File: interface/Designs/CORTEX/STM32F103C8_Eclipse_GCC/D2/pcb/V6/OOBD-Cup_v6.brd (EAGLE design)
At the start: 160 x 100 mm, 42 parts, among them IC1 MC34063-SO, IC2 BTM-182, IC3 PCA82C250T, T1 BC817, T100 BC817, T101 BC817, U1 STM32F10XTXU6

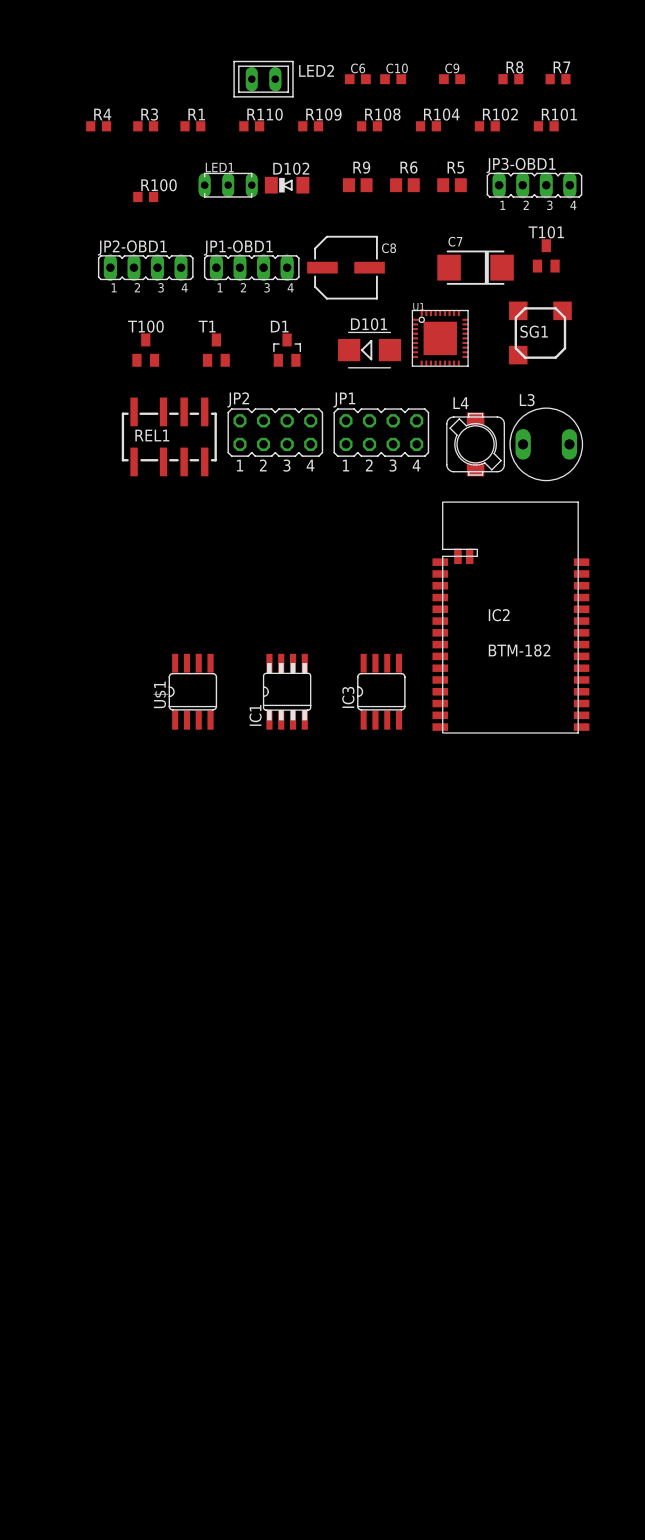
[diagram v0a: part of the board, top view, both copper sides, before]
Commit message: K-Line interface connected
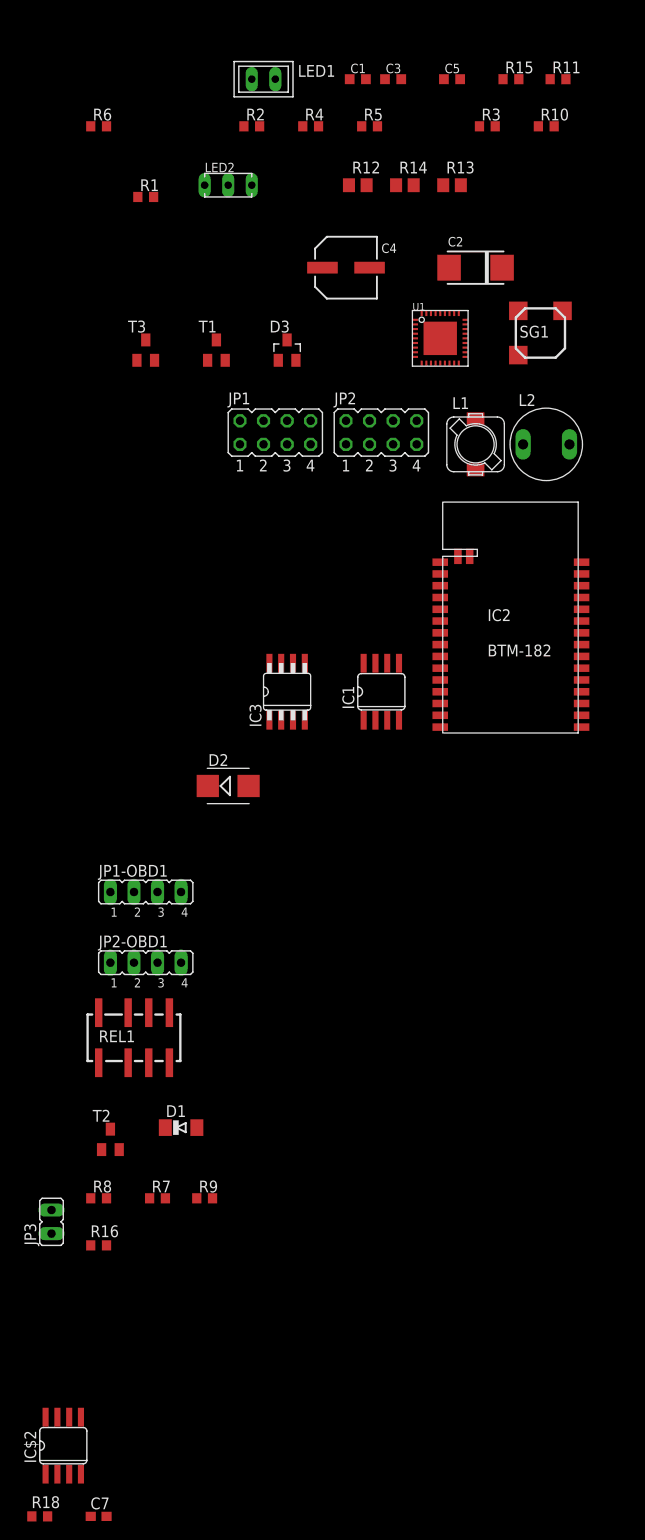
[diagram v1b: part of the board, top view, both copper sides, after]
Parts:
- removed D101: B140, diode:SMB
- removed D102: 1N4148, diode:MINIMELF
- removed JP3-OBD1: (no value), jumper:JP4
- removed R100, R102: 82R, rcl:R0603
- removed R104, R109: 4k7, rcl:R0603
- removed R108: 10k, rcl:R0603
- removed T101: BC817, transistor:SOT23
- removed U$1: SI9241AEY, Si9241AEY:SO08
- added C2: 220µF, rc-master:C6032-TE-C
- added D2: B140, diode:SMB
- added D3: BAS40, diode:SOT23
- added IC$2: SI9243AEY, Vishay_ISO9141:SO08
- added JP3: (no value), jumper:JP1
- added R11: 3k3, rcl:R0603
- added R12, R13, R14: 1R, rcl:R0805
- added R15: 5k6, rcl:R0603
- added R16: 120R, resistor:R0603
- added R18: 510R, resistor:R0603
- added T2: BC817, transistor:SOT23
- C7: value 220µF -> 10nF; device rc-master:C6032-TE-C -> resistor:C0603
- D1: value BAS40 -> 1N4148; device diode:SOT23 -> diode:MINIMELF
- IC1: value MC34063-SO -> PCA82C250T; device mc34063:SO8 -> can:SO08
- IC3: value PCA82C250T -> MC34063-SO; device can:SO08 -> mc34063:SO8
- JP1: value SPI / SD-Card -> Program
- JP2: value Program -> SPI / SD-Card
- LED1: value Rt/Gr -> Blue; device led:DUOLED2X5 -> led:U57X32
- LED2: value Blue -> Rt/Gr; device led:U57X32 -> led:DUOLED2X5
- R1: value 180k -> 82R
- R3: value 47k -> 82R
- R4: value 10k -> 4k7
- R5, R6: value 1R -> 10k; device rcl:R0805 -> rcl:R0603
- R7: value 3k3 -> 4k7
- R8: value 5k6 -> 180k
- R9: value 1R -> 47k; device rcl:R0805 -> rcl:R0603
- moved C7 140.6 mm to (-66.0, -83.8)
- moved R8 128.6 mm to (-66.0, -49.5)
- moved R7 128.1 mm to (-59.7, -49.5)
- moved R9 110.5 mm to (-54.6, -49.5)
- moved D1 84.6 mm to (-57.1, -41.9)
- moved JP2-OBD1 74.9 mm to (-61.0, -24.1)
- moved JP1-OBD1 68.3 mm to (-61.0, -16.5)
- moved REL1 64.9 mm to (-62.2, -31.8)
- moved R3 36.8 mm to (-24.1, 66.0)
- moved R6 33.6 mm to (-66.0, 66.0)
- moved R4 22.9 mm to (-43.2, 66.0)
- moved LED1 12.0 mm to (-48.3, 71.1)
- moved LED2 12.0 mm to (-52.1, 59.7)
- moved JP1 11.4 mm to (-47.0, 33.0)
- moved JP2 11.4 mm to (-35.6, 33.0)
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- renumbered C10 to C3, C6 to C1, C8 to C4, C9 to C5, L3 to L2, L4 to L1, R101 to R10, R110 to R2, T100 to T3
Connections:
- removed net 12V_DOUT1: C4.+, C5.1, IC1.6, R5.2, R6.2, R9.2
- removed net MODE2: R104.1
- removed net N$19: R1.1, R3.2
- removed net N$21: REL1.3
- removed net N$22: REL1.6
- removed net PWM+: JP3-OBD1.3
- removed net PWM-: JP3-OBD1.4
- removed net VDD: IC2.P$14
- new net +5V: IC$2.3
- new net CAN-RXD: IC1.4
- new net CAN-TXD: IC1.1
- new net CAN_SW: R7.1
- new net N$16: JP3.2, R16.1
- new net N$5: IC1.7, R16.2, REL1.3
- new net REL_DIAG: R8.1, R9.2
- new net RX_K: IC$2.1
- new net RX_L: IC$2.2
- new net TX: IC$2.4
- new net VBAT: D2.A, IC$2.7, IC2.P$14, JP2-OBD1.4, R18.2
- net +12V: now also C4.+, C5.1, D1.C, D2.C, IC3.6, LED1.A, R12.2, R13.2, R14.2; no longer D101.A, D102.C, JP2-OBD1.4, LED2.A
- net +3V3: now also C2.+, JP1.1, R15.2; no longer C7.+, JP2.1, R8.2
- net A0: now also JP2.3; no longer JP1.3
- net BOOT0: now also JP1.2; no longer JP2.2
- net CS: now also JP2.2; no longer JP1.2
- net CTS: now also JP2.5; no longer JP1.5
- net GND: now also C2.-, C7.2, D3.1, IC$2.5, IC1.2, IC1.8, IC3.4, JP1.3, LED2.K, R11.2, R5.2, R6.2, R9.1, T2.2; no longer C7.-, D1.1, IC1.4, IC3.2, JP2.3, LED1.K, R108.2, R3.1, R4.2, R7.2, T101.2
- net K-LINE: now also C7.1, IC$2.6, JP2-OBD1.2, R18.1; no longer JP3-OBD1.2
- net L-LINE: now also IC$2.8, JP2-OBD1.1; no longer JP3-OBD1.1
- net MISO: now also JP2.6; no longer JP1.6
- net MODE1: now also R6.1; no longer R4.1
- net MOSI: now also JP2.8; no longer JP1.8
- net N$10: now also R4.2; no longer R109.2
- net N$11: now also IC3.3; no longer IC1.3
- net N$12: now also IC3.1, IC3.7, IC3.8, R12.1, R13.1, R14.1; no longer IC1.1, IC1.7, IC1.8, R5.1, R6.1, R9.1
- net N$13: now also IC3.5, R11.1, R15.1; no longer IC1.5, R7.1, R8.1
- net N$14: now also D3.3, IC3.2; no longer D1.3, IC1.2
- net N$20: now also R7.2, T2.1; no longer R104.2, T101.1
- net N$27: now also D1.A, R8.2, T2.3; no longer D102.A, R1.2, T101.3
- net N$3: now also IC1.6, JP3.1, REL1.6; no longer D101.C
- net N$4: now also LED2.AR, R3.2; no longer LED1.AR, R102.2
- net N$6: now also LED2.AG, R1.2; no longer LED1.AG, R100.2
- net N$7: now also LED1.K, R4.1; no longer LED2.K, R109.1
- net RTS: now also JP2.7; no longer JP1.7
- net SCK: now also JP2.4; no longer JP1.4
- net VCC: now also IC1.3; no longer IC3.3

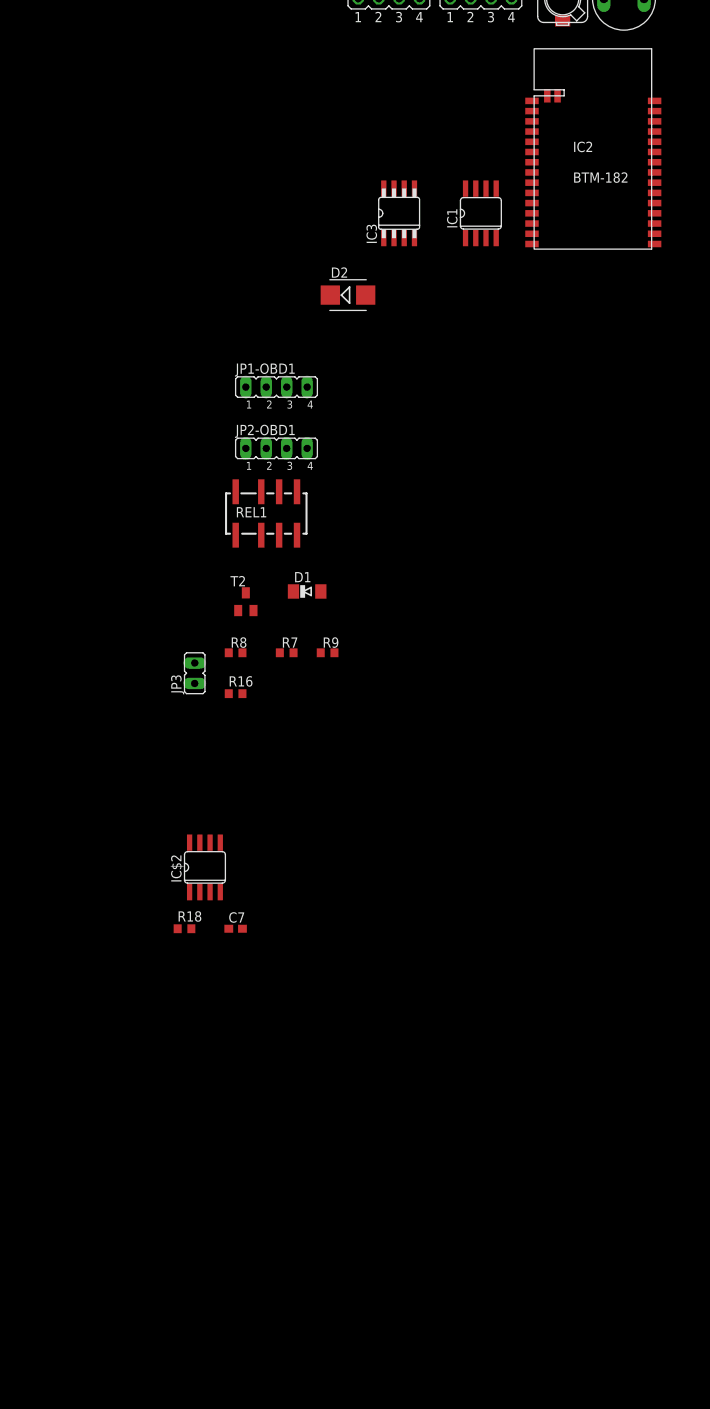
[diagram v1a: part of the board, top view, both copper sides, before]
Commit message: add further parts for STM32F103T8
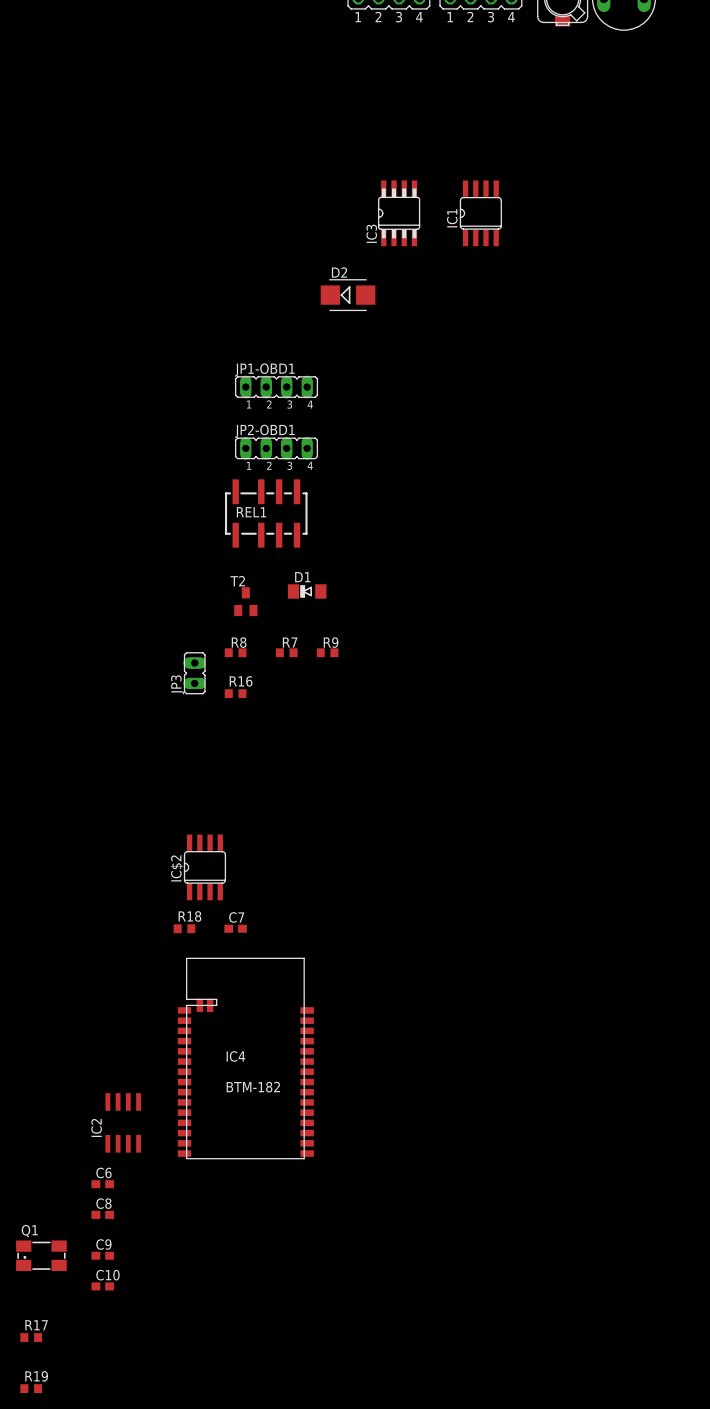
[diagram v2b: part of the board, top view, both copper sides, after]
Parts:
- added C10, C9: 15p, resistor:C0603
- added C6, C8: 100n, resistor:C0603
- added IC4: BTM-182, BTM182:BTM-182
- added Q1: 8MHz, crystal:CTS406
- added R17, R19: 10k, resistor:R0603
- IC2: value BTM-182 -> 78L05SMD; device BTM182:BTM-182 -> linear:SO08
- moved IC2 132.9 mm to (-80.0, -108.0)
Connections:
- removed net VCC: IC1.3
- removed net VDDA: U1.6
- removed net VDD_1: U1.19
- removed net VDD_2: U1.27
- removed net VDD_3: U1.1
- removed net VDD_USB: IC2.P$16
- removed net VSSA: U1.5
- removed net VSS_1: U1.18
- removed net VSS_2: U1.26
- removed net VSS_3: U1.36
- new net BTM_RX: IC4.P$10, JP1.8
- new net BTM_TX: IC4.P$9, JP1.6
- new net BT_RES-: IC4.P$21
- new net N$1: C10.2, Q1.1, U1.2
- new net N$2: C9.2, Q1.3, U1.3
- new net RESET-: JP1.4, R17.1, U1.4
- new net STM_RXD: JP1.5, U1.22
- new net STM_TXD: JP1.7, U1.21
- net +12V: now also C6.1, IC2.8
- net +3V3: now also IC4.P$14, IC4.P$16, R17.2, U1.1, U1.19, U1.27, U1.6
- net +5V: now also C8.1, IC1.3, IC2.1
- net BOOT0: now also R19.2, U1.35
- net GND: now also C10.1, C6.2, C8.2, C9.1, IC2.2, IC2.3, IC2.6, IC2.7, IC4.P$15, R19.1, U1.18, U1.26, U1.36, U1.5; no longer IC2.P$15
- net MODE1: now also R5.1
- net RX_K: now also U1.10
- net TX: now also U1.9
- net VBAT: no longer IC2.P$14

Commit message: OOBD-Cup_v6 ready for design review and optimization
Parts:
- removed JP2: SPI / SD-Card, jumper:JP4Q
- added C11: (no value), resistor:C0603
- added R20: 130k, resistor:R0603
- added R21: 27k, resistor:R0603
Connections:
- removed net A0: JP2.3, R10.1
- removed net CS: JP2.2
- removed net CTS: JP2.5
- removed net MISO: JP2.6
- removed net MOSI: JP2.8
- removed net N$8: R2.1
- removed net RTS: JP2.7
- removed net SCK: JP2.4
- new net BUZZER: R10.1, U1.13
- new net LED1: R3.1, U1.32
- new net LED2: R1.1, U1.31
- new net LED_BLUE: R2.1, U1.14
- new net N$15: C11.1, R20.1, R21.2, U1.15
- new net N$18: R5.1, U1.28
- net +12V: now also R20.2
- net GND: now also C11.2, R21.1, U1.17
- net MODE1: now also U1.25; no longer R5.1
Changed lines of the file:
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@@
 <elements>
 <element name="JP1" library="jumper" package="JP4Q" value="Program" x="-46.99" y="33.02"/>
-<element name="JP2" library="jumper" package="JP4Q" value="SPI / SD-Card" x="-35.56" y="33.02"/>
 <element name="LED2" library="led" package="DUOLED2X5" value="Rt/Gr" x="-52.07" y="59.69"/>
 <element name="LED1" library="led" package="U57X32" value="Blue" x="-48.26" y="71.12"/>
@@
 <element name="R17" library="resistor" package="R0603" value="10k" x="-91.44" y="-134.62"/>
 <element name="R19" library="resistor" package="R0603" value="10k" x="-91.44" y="-140.97"/>
+<element name="R20" library="resistor" package="R0603" value="130k" x="-91.44" y="-147.32"/>
+<element name="R21" library="resistor" package="R0603" value="27k" x="-91.44" y="-153.67"/>
+<element name="C11" library="resistor" package="C0603" value="" x="-91.44" y="-158.75"/>
 </elements>
 <signals>
@@
 <contactref element="C10" pad="1"/>
 <contactref element="R19" pad="1"/>
+<contactref element="U1" pad="17"/>
+<contactref element="R21" pad="1"/>
+<contactref element="C11" pad="2"/>
+<wire x1="-92.29" y1="-153.67" x2="-90.59" y2="-158.75" width="0" layer="19" extent="1-1"/>
+<wire x1="-92.29" y1="-140.97" x2="-92.29" y2="-153.67" width="0" layer="19" extent="1-1"/>
 <wire x1="-83.4" y1="-128.27" x2="-92.29" y2="-140.97" width="0" layer="19" extent="1-1"/>
 <wire x1="-83.4" y1="-124.46" x2="-83.4" y2="-128.27" width="0" layer="19" extent="1-1"/>
@@
 <wire x1="-26.51" y1="44.68" x2="-31.21" y2="45.88" width="0" layer="19" extent="1-1"/>
 <wire x1="-27.21" y1="40.48" x2="-26.51" y2="44.68" width="0" layer="19" extent="1-1"/>
+<wire x1="-27.71" y1="40.48" x2="-27.21" y2="40.48" width="0" layer="19" extent="1-1"/>
 <wire x1="-28.2575" y1="50.8" x2="-31.21" y2="45.88" width="0" layer="19" extent="1-1"/>
 <wire x1="-35.98" y1="66.04" x2="-36.83" y2="50.8" width="0" layer="19" extent="1-1"/>
@@
 <contactref element="IC2" pad="8"/>
 <contactref element="C6" pad="1"/>
+<contactref element="R20" pad="2"/>
+<wire x1="-83.4" y1="-115.57" x2="-90.59" y2="-147.32" width="0" layer="19" extent="1-1"/>
 <wire x1="-81.915" y1="-105.35" x2="-83.4" y2="-115.57" width="0" layer="19" extent="1-1"/>
 <wire x1="-58.85" y1="-41.91" x2="-81.915" y2="-105.35" width="0" layer="19" extent="1-1"/>
@@
 <wire x1="-30.71" y1="45.88" x2="-50.8" y2="34.29" width="0" layer="19" extent="1-1"/>
 </signal>
-<signal name="MOSI">
-<contactref element="JP2" pad="8"/>
-</signal>
-<signal name="MISO">
-<contactref element="JP2" pad="6"/>
-</signal>
-<signal name="SCK">
-<contactref element="JP2" pad="4"/>
-</signal>
-<signal name="CS">
-<contactref element="JP2" pad="2"/>
-</signal>
-<signal name="RTS">
-<contactref element="JP2" pad="7"/>
-</signal>
-<signal name="CTS">
-<contactref element="JP2" pad="5"/>
-</signal>
-<signal name="A0">
-<contactref element="JP2" pad="3"/>
-<contactref element="R10" pad="1"/>
-<wire x1="-36.83" y1="31.75" x2="-18.63" y2="66.04" width="0" layer="19" extent="1-1"/>
-</signal>
 <signal name="N$4">
 <contactref element="R3" pad="2"/>
@@
 <wire x1="-44.03" y1="66.04" x2="-46.99" y2="71.12" width="0" layer="19" extent="1-1"/>
 </signal>
-<signal name="N$8">
-<contactref element="R2" pad="1"/>
-</signal>
 <signal name="N$23">
 <contactref element="T3" pad="3"/>
@@
 </signal>
 <signal name="MODE1">
+<contactref element="U1" pad="25"/>
 <contactref element="R6" pad="1"/>
-<contactref element="R5" pad="1"/>
-<wire x1="-66.89" y1="66.04" x2="-37.68" y2="66.04" width="0" layer="19" extent="1-1"/>
+<wire x1="-66.89" y1="66.04" x2="-26.51" y2="44.18" width="0" layer="19" extent="1-1"/>
 </signal>
 <signal name="N$9">
@@
 <wire x1="-26.51" y1="42.68" x2="-45.72" y2="31.75" width="0" layer="19" extent="1-1"/>
 </signal>
+<signal name="N$15">
+<contactref element="R20" pad="1"/>
+<contactref element="R21" pad="2"/>
+<contactref element="U1" pad="15"/>
+<contactref element="C11" pad="1"/>
+<wire x1="-90.59" y1="-153.67" x2="-92.29" y2="-158.75" width="0" layer="19" extent="1-1"/>
+<wire x1="-92.29" y1="-147.32" x2="-90.59" y2="-153.67" width="0" layer="19" extent="1-1"/>
+<wire x1="-28.71" y1="40.48" x2="-92.29" y2="-147.32" width="0" layer="19" extent="1-1"/>
+</signal>
+<signal name="BUZZER">
+<contactref element="U1" pad="13"/>
+<contactref element="R10" pad="1"/>
+<wire x1="-29.71" y1="40.48" x2="-18.63" y2="66.04" width="0" layer="19" extent="1-1"/>
+</signal>
+<signal name="LED_BLUE">
+<contactref element="U1" pad="14"/>
+<contactref element="R2" pad="1"/>
+<wire x1="-29.21" y1="40.48" x2="-50.38" y2="66.04" width="0" layer="19" extent="1-1"/>
+</signal>
+<signal name="LED2">
+<contactref element="R1" pad="1"/>
+<contactref element="U1" pad="31"/>
+<wire x1="-61.81" y1="58.42" x2="-28.71" y2="45.88" width="0" layer="19" extent="1-1"/>
+</signal>
+<signal name="LED1">
+<contactref element="R3" pad="1"/>
+<contactref element="U1" pad="32"/>
+<wire x1="-29.21" y1="45.88" x2="-24.98" y2="66.04" width="0" layer="19" extent="1-1"/>
+</signal>
+<signal name="N$18">
+<contactref element="U1" pad="28"/>
+<contactref element="R5" pad="1"/>
+<wire x1="-27.21" y1="45.88" x2="-37.68" y2="66.04" width="0" layer="19" extent="1-1"/>
+</signal>
 </signals>
